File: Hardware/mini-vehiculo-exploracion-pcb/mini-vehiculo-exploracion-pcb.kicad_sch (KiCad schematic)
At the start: 19 parts, among them IC1 BME690, J1 ArducamMINIOV2640, U1 BNO086, U2 ESP32-S3-WROOM-1, Y1 830003000

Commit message: creacion electrical sheet
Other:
- added sheet Electrical (electrical.kicad_sch)
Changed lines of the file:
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@@
+		)
+	)
+	(sheet
+		(at 205.74 130.81)
+		(size 33.02 16.51)
+		(exclude_from_sim no)
+		(in_bom yes)
+		(on_board yes)
+		(dnp no)
+		(fields_autoplaced yes)
+		(stroke
+			(width 0.1524)
+			(type solid)
+		)
+		(fill
+			(color 0 0 0 0.0000)
+		)
+		(property "Sheetname" "Electrical"
+			(at 205.74 130.0984 0)
+			(effects
+				(font
+					(size 1.27 1.27)
+				)
+				(justify left bottom)
+			)
+		)
+		(property "Sheetfile" "electrical.kicad_sch"
+			(at 205.74 147.9046 0)
+			(effects
+				(font
+					(size 1.27 1.27)
+				)
+				(justify left top)
+			)
+		)
+		(instances
+			(project "mini-vehiculo-exploracion-pcb"
+				(path "/3cb3b833-c38f-47b4-b7e9-f0e6337b7613"
+					(page "3")
+				)
+			)
 		)
 	)

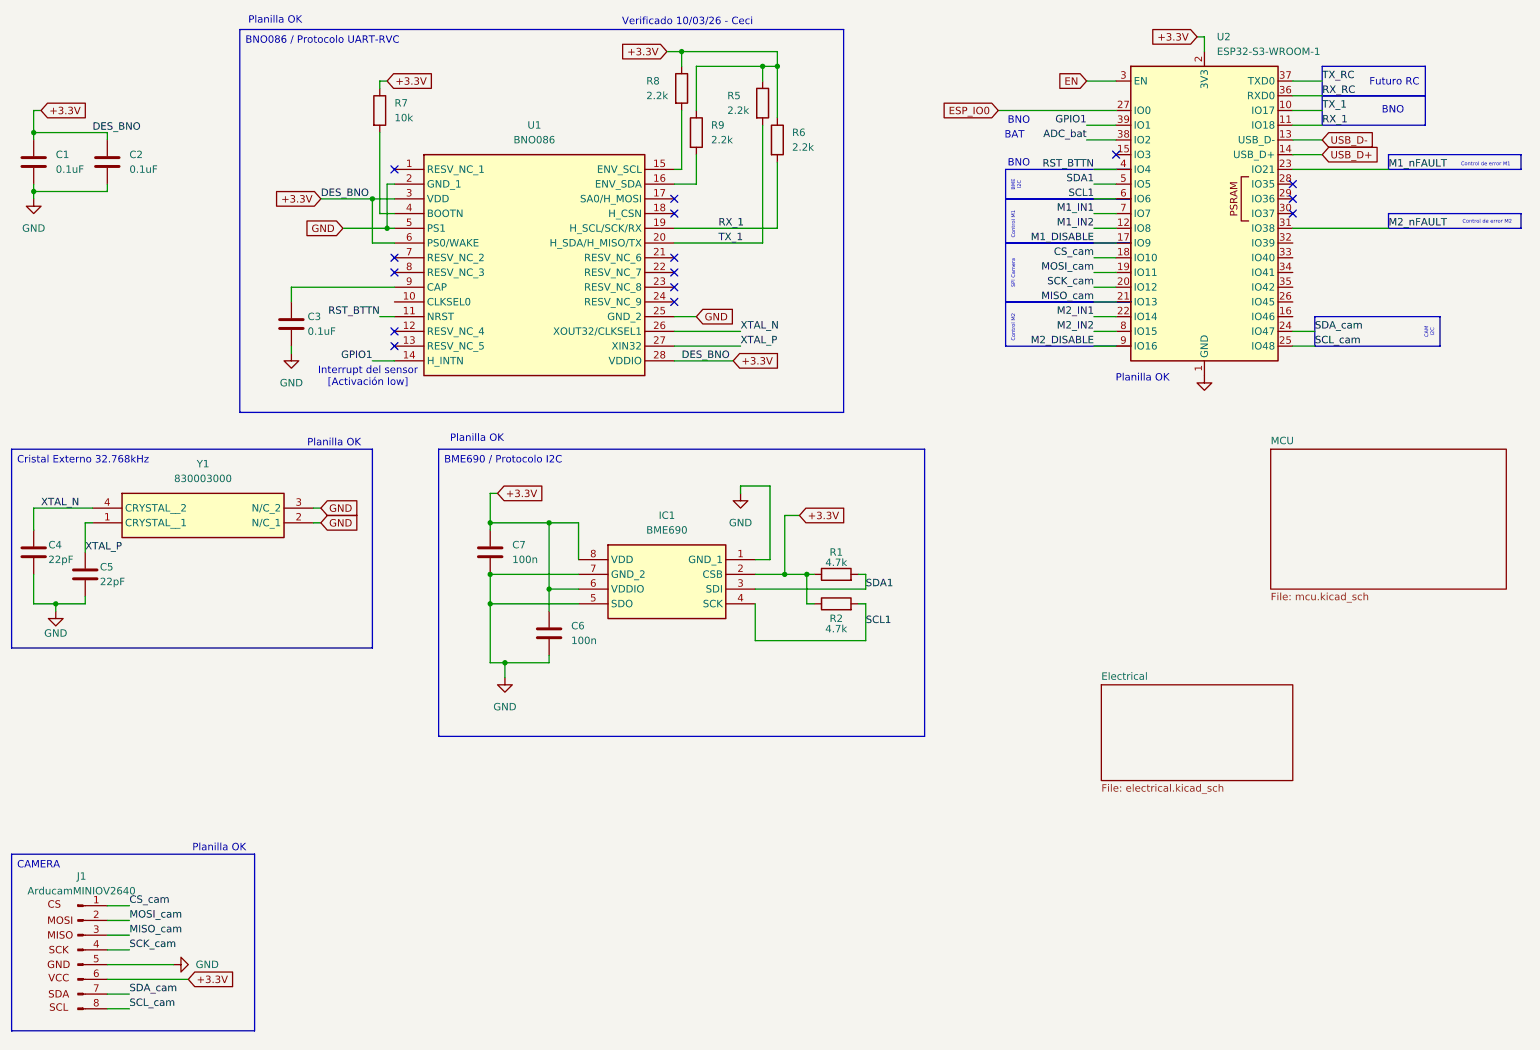
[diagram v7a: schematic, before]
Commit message: Add pin headers, run ERC
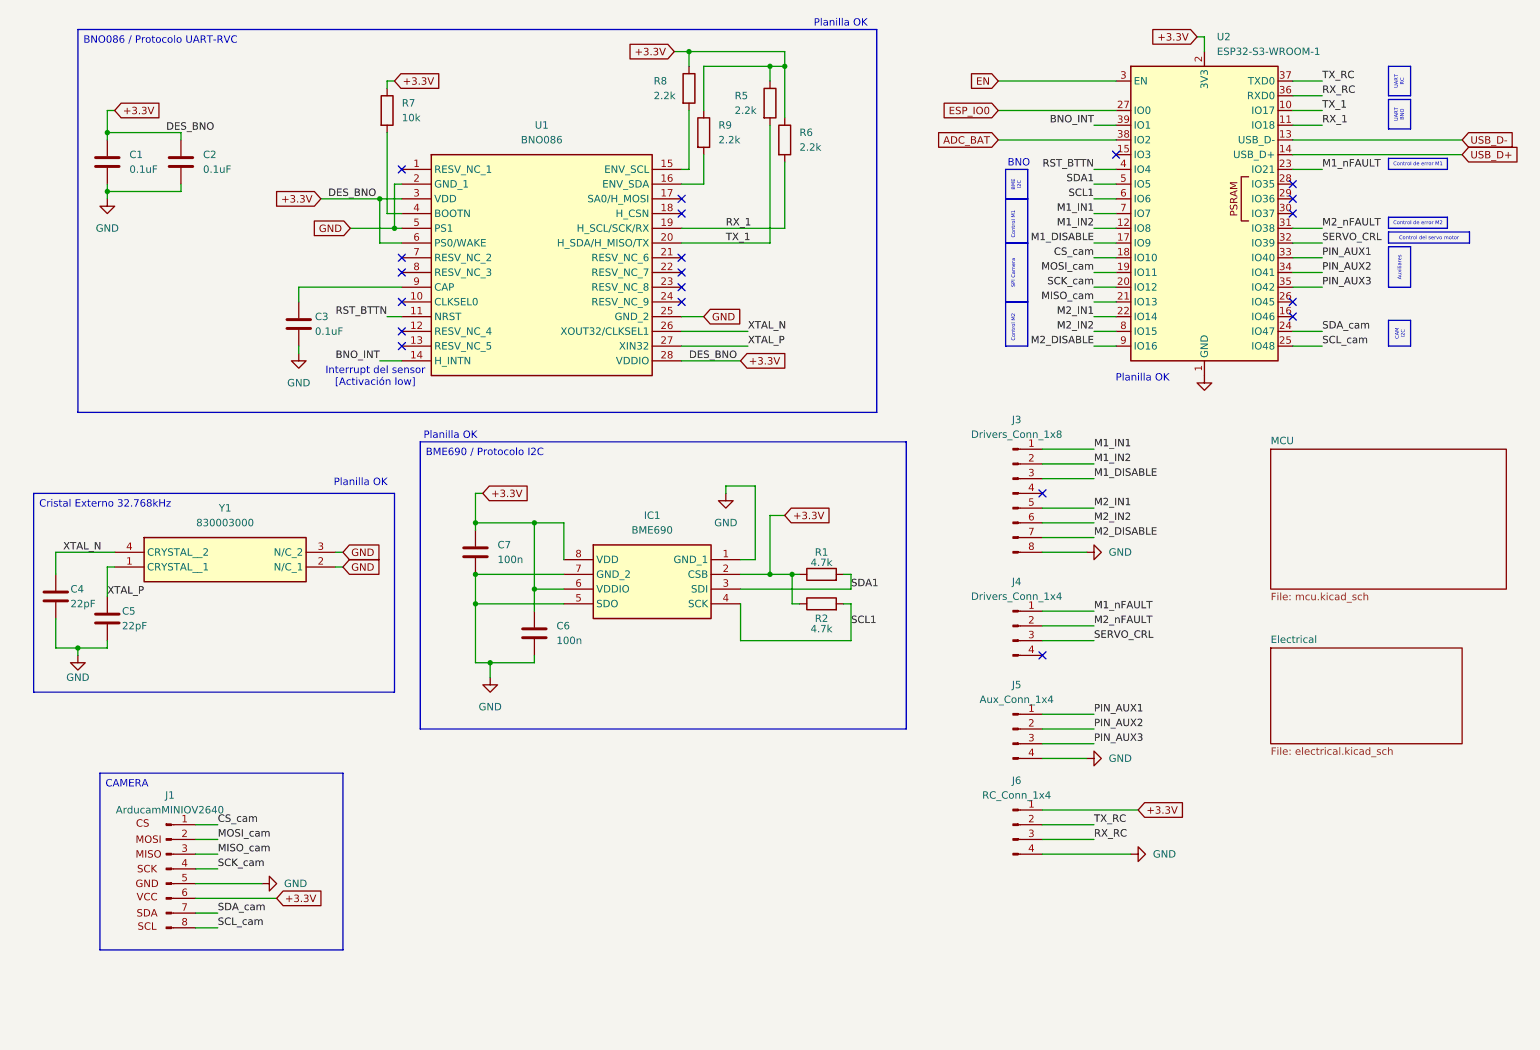
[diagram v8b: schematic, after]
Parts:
- added J3: Drivers_Conn_1x8, symbol Connector:Conn_01x08_Pin
- added J4: Drivers_Conn_1x4, symbol Connector:Conn_01x04_Pin
- added J5: Aux_Conn_1x4, symbol Connector:Conn_01x04_Pin
- added J6: RC_Conn_1x4, symbol Connector:Conn_01x04_Pin
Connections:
- net +3.3V: now also J6.1 (Pin_1)
- net GND: now also J3.8 (Pin_8), J5.4 (Pin_4), J6.4 (Pin_4)
- net M1_DISABLE: now also J3.3 (Pin_3)
- net M1_IN1: now also J3.1 (Pin_1)
- net M1_IN2: now also J3.2 (Pin_2)
- net M1_nFAULT: now also J4.1 (Pin_1)
- net M2_DISABLE: now also J3.7 (Pin_7)
- net M2_IN1: now also J3.5 (Pin_5)
- net M2_IN2: now also J3.6 (Pin_6)
- net M2_nFAULT: now also J4.2 (Pin_2)
- net RX_RC: now also J6.3 (Pin_3)
- net TX_RC: now also J6.2 (Pin_2)
- net SERVO_CRL: now reaches U2.32 (IO39)
- net SERVO_CRL: now also J4.3 (Pin_3)
- net PIN_AUX1: now reaches U2.33 (IO40)
- net PIN_AUX1: now also J5.1 (Pin_1)
- net PIN_AUX2: now reaches U2.34 (IO41)
- net PIN_AUX2: now also J5.2 (Pin_2)
- net PIN_AUX3: now reaches U2.35 (IO42)
- net PIN_AUX3: now also J5.3 (Pin_3)
- net ADC_bat renamed ADC_BAT
- net GPIO1 renamed BNO_INT
- no-connect marks 15 -> 20
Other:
- note removed: "BAT"
- note removed: "Futuro RC"
- note removed: "Verificado 10/03/26 - Ceci"
- moved on the sheet: C1, C2, C3, C4, C5, C6, C7, IC1, J1, R1, R2, R5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
